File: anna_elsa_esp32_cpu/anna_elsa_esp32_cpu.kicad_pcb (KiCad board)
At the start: 4 copper layers, 170.2 x 106.7 mm, 115 parts, among them J1 REEL_RIGHT, J10 CREDIT_DISPLAY, J11 SPKR_R, J12 HEADER_6x2, J14 DOOR_SW, J2 REEL_CENTRE, J22 BTN_SWITCHES, J23 BTN_LAMPS, J3 REEL_LEFT, J4 LED / VFD, J5 LED_STRIP, J6 ATX-24, J7 HOPPER, J8 COIN_VALIDATOR, J9 SPKR_L, Q1 BC846, Q2 BC856, Q3 ULN2803ADWR, Q4 BSS138, Q7 BSS138, SW1 RESET, SW2 BOOT, U1 ESP32-WROOM-32E(16M), U10 SN74LVC1G17, U11 SN74LVC1G17, U12 Boost_Converter, U2 SN74LVC1G17, U3 TAS5825MRHB, U4 DS3231M, U5 SN74LVC1G17, U6 SN74LVC1G17, U7 SN74LVC1G17, U8 MCP23017-E_SO, U9 SN74LVC1G17

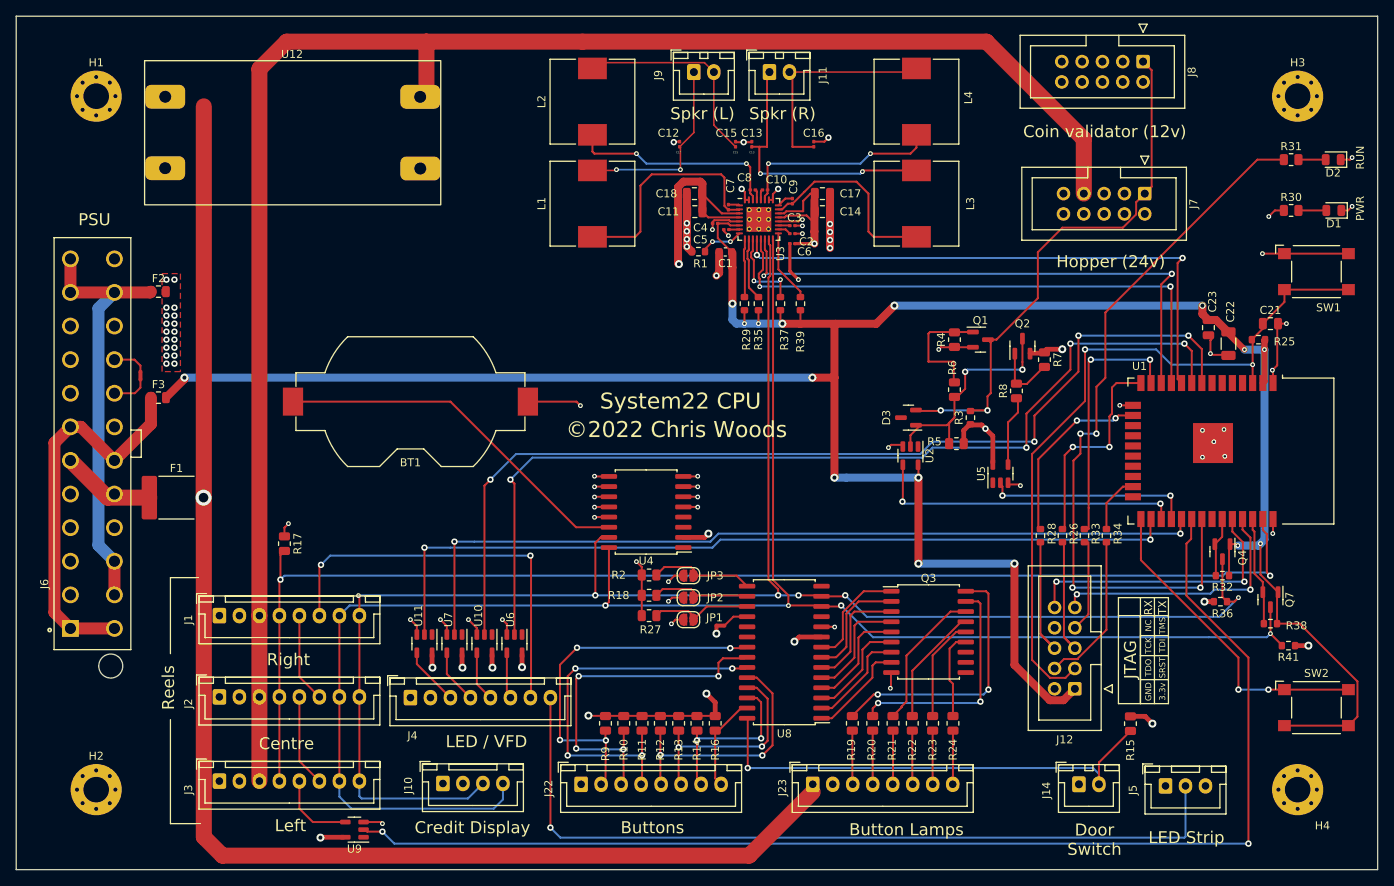
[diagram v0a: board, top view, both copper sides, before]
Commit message: Added current cpu pcb and removed old
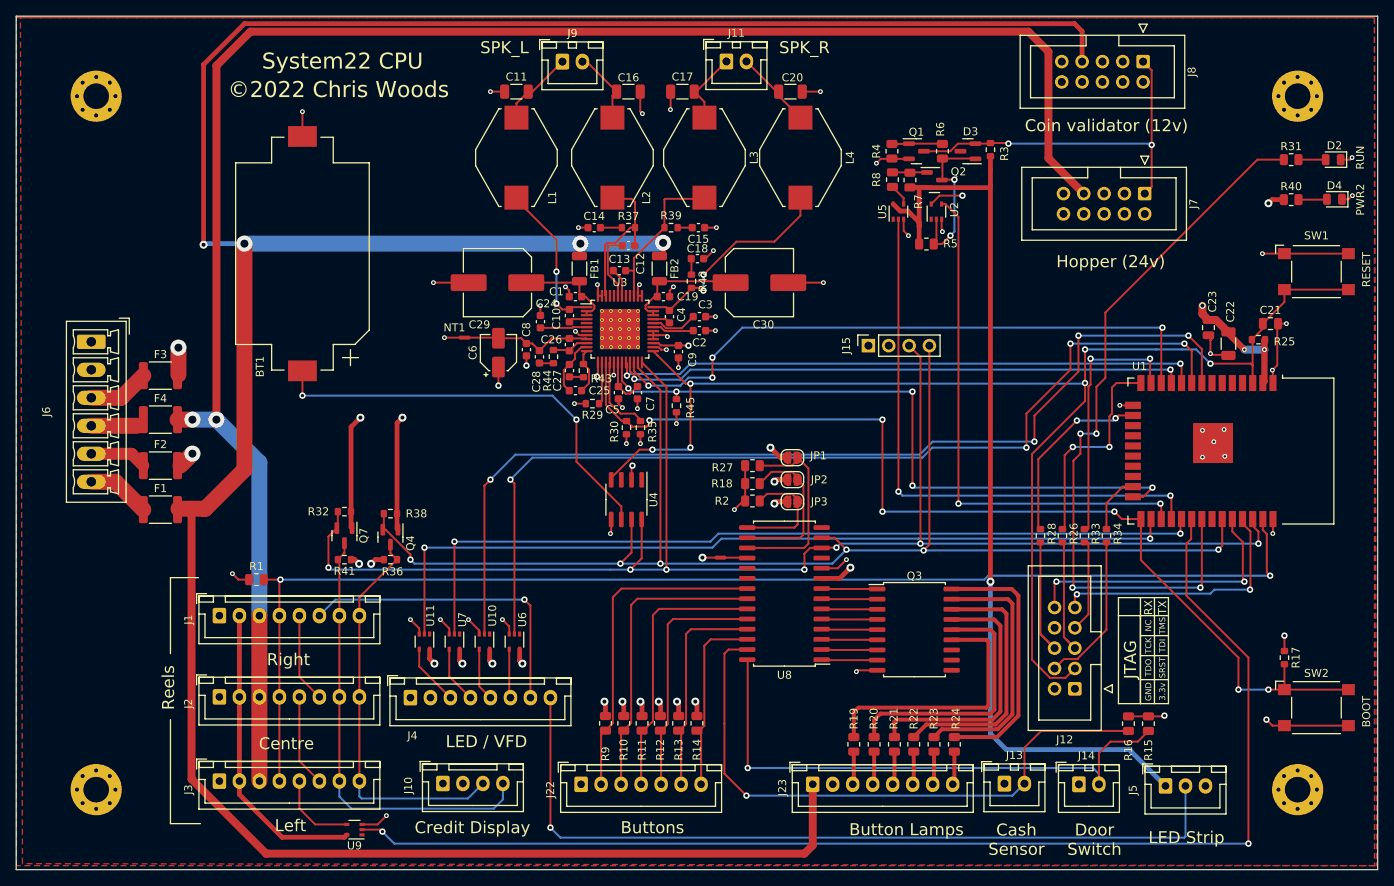
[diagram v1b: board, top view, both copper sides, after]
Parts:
- removed D1: PWR, LED_SMD:LED_0805_2012Metric
- removed U12: Boost_Converter, Converter_DCDC:Boost_Converter
- added C19: 100nF/50v, Capacitor_SMD:C_0603_1608Metric, F.Cu at (126.6, 55.4)
- added C20: 680nF/50V, Capacitor_SMD:C_1206_3216Metric, F.Cu at (142.5, 29.8)
- added C24: 220pF/50V, Capacitor_SMD:C_0603_1608Metric, F.Cu at (111.2, 58.5)
- added C25: 4.7nF/50V, Capacitor_SMD:C_0603_1608Metric, F.Cu at (115.6, 67.1)
- added C26: 4.7nF/50V, Capacitor_SMD:C_0603_1608Metric, F.Cu at (114.9, 61.4)
- added C27: 47nF/16v, Capacitor_SMD:C_0603_1608Metric, F.Cu at (114.9, 64.6)
- added C28: 47nF/16v, Capacitor_SMD:C_0603_1608Metric, F.Cu at (111.1, 62.9)
- added C29: 220µF/35v, Capacitor_SMD:C_Elec_8x10.2, F.Cu at (105.9, 53.6)
- added C30: 220µF/35v, Capacitor_SMD:C_Elec_8x10.2, F.Cu at (138.6, 53.6)
- added D4: PWR2, LED_SMD:LED_0805_2012Metric, F.Cu at (210.5, 43.2)
- added F4: 2A 30V, Fuse:Fuse_1812_4532Metric, F.Cu at (63.8, 70.8)
- added FB1: 120Ohm@100MHz 4A, Inductor_SMD:L_1206_3216Metric, F.Cu at (116.1, 51.9)
- added FB2: 120Ohm@100MHz 4A, Inductor_SMD:L_1206_3216Metric, F.Cu at (126.1, 51.9)
- added J13: CASH_LVL, Connector_JST:JST_XH_B2B-XH-A_1x02_P2.50mm_Vertical, F.Cu at (169.2, 116.2)
- added J15: Oled, Connector_PinSocket_2.54mm:PinSocket_1x04_P2.54mm_Vertical, F.Cu at (152.2, 61.5)
- added R40: 180, Resistor_SMD:R_0805_2012Metric, F.Cu at (205.1, 43.2)
- added R42: 18, Resistor_SMD:R_0603_1608Metric, F.Cu at (130.1, 53.5)
- added R43: 470, Resistor_SMD:R_0603_1608Metric, F.Cu at (116.6, 64.6)
- added R44: 470, Resistor_SMD:R_0603_1608Metric, F.Cu at (112.9, 62.9)
- added R45: 10k, Resistor_SMD:R_0603_1608Metric, F.Cu at (128.2, 69.0)
- BT1: footprint Battery:BatteryHolder_Keystone_1058_1x2032 -> Battery:BatteryHolder_Keystone_1060_1x2032
- C1: value 4.7µF/16v -> 100nF/50v
- C10: value 0.47µF -> 33nF/50V; footprint Capacitor_SMD:C_0201_0603Metric -> Capacitor_SMD:C_0603_1608Metric
- C11, C17: value 22µF/35v -> 680nF/50V; footprint Capacitor_SMD:C_0805_2012Metric -> Capacitor_SMD:C_1206_3216Metric
- C12, C13: value 0.68µF -> 33nF/50V; footprint Capacitor_SMD:C_0201_0603Metric -> Capacitor_SMD:C_0603_1608Metric
- C14, C18: value 22µF/35v -> 330pF/50V; footprint Capacitor_SMD:C_0805_2012Metric -> Capacitor_SMD:C_0603_1608Metric
- C15: value 0.68µF -> 330pF/50V; footprint Capacitor_SMD:C_0201_0603Metric -> Capacitor_SMD:C_0603_1608Metric
- C16: value 0.68µF -> 680nF/50V; footprint Capacitor_SMD:C_0201_0603Metric -> Capacitor_SMD:C_1206_3216Metric
- C2, C3: value 1µF -> 100nF/50v; footprint Capacitor_SMD:C_0201_0603Metric -> Capacitor_SMD:C_0603_1608Metric
- C23: value 1µF/50V -> 1µF/50v
- C4: value 0.1µF/16v -> 33nF/50V; footprint Capacitor_SMD:C_0201_0603Metric -> Capacitor_SMD:C_0603_1608Metric
- C5: value 1µF -> 4.7µF/16v; footprint Capacitor_SMD:C_0201_0603Metric -> Capacitor_SMD:C_0603_1608Metric
- C6: value 0.1µF/16v -> 10µF/6.3v; footprint Capacitor_SMD:C_0201_0603Metric -> Capacitor_SMD:CP_Elec_4x5.4
- C7, C8, C9: value 0.47µF -> 100nF/50v; footprint Capacitor_SMD:C_0201_0603Metric -> Capacitor_SMD:C_0603_1608Metric
- F1: value 2A 15V -> 2A 30V; footprint Fuse:Fuse_2920_7451Metric -> Fuse:Fuse_1812_4532Metric
- F2: value 2.6A 6V -> 2A 30V; footprint Fuse:Fuse_0805_2012Metric -> Fuse:Fuse_1812_4532Metric
- F3: value Polyfuse -> 2A 30V; footprint Fuse:Fuse_0805_2012Metric -> Fuse:Fuse_1812_4532Metric
- J11: value SPKR_R -> SPK_R
- J12: value HEADER_6x2 -> JTAG
- J22: footprint Connector_JST:JST_XH_B8B-XH-A_1x08_P2.50mm_Vertical -> Connector_JST:JST_XH_B7B-XH-A_1x07_P2.50mm_Vertical
- J6: value ATX-24 -> PSU; footprint Connector_TE-Connectivity:TE_1-1775099-3 -> Connector_Phoenix_MC:PhoenixContact_MCV_1,5_6-G-3.5_1x06_P3.50mm_Vertical
- J9: value SPKR_L -> SPK_L
- L1, L2, L3, L4: value 10µH / 4.4A / 0.03Ohm -> 15µH; footprint Inductor_SMD:L_10.4x10.4_H4.8 -> Inductor_SMD:L_SigTra_SC3316F
- Q1: value BC846 -> SS8050
- Q2: value BC856 -> SS8850
- R1: value 0 -> 4k7; footprint Resistor_SMD:R_0603_1608Metric -> Resistor_SMD:R_0805_2012Metric
- R17: value 4k7 -> 10k; footprint Resistor_SMD:R_0805_2012Metric -> Resistor_SMD:R_0603_1608Metric
- R29: value 10k -> 15.0k
- R30: value 220 -> 10k; footprint Resistor_SMD:R_0805_2012Metric -> Resistor_SMD:R_0603_1608Metric
- R35: value 10k -> 18.2k
- R37, R39: value 10k -> 18
- U1: value ESP32-WROOM-32E(16M) -> ESP32-WROOM-32D(16M)
- U10, U11, U2, U5, U6, U7, U9: footprint Package_TO_SOT_SMD:SOT-23-5 -> Package_TO_SOT_SMD:SOT-353_SC-70-5
- U3: value TAS5825MRHB -> TAS5731PHP; footprint Package_DFN_QFN:VQFN-32-1EP_5x5mm_P0.5mm_EP3.1x3.1mm_ThermalVias -> Package_QFP:TQFP-48-1EP_7x7mm_P0.5mm_EP5x5mm_ThermalVias
- U4: footprint Package_SO:SOIC-16W_7.5x10.3mm_P1.27mm -> Package_SO:SOIC-8_3.9x4.9mm_P1.27mm
- U8: value MCP23017-E_SO -> MCP23017T-E/SO
- moved R17 125.8 mm to (204.2, 100.5)
- moved R41 118.5 mm to (86.8, 88.2)
- moved R38 116.6 mm to (86.8, 82.2)
- moved Q7 116.0 mm to (86.8, 85.2)
- moved R32 104.3 mm to (92.5, 82.5)
- moved Q4 104.0 mm to (92.5, 85.4)
- moved R36 103.9 mm to (92.5, 88.2)
- moved R30 87.4 mm to (122.0, 71.8), turned to 90 degrees
- moved R1 68.8 mm to (75.8, 90.8), turned to 0 degrees
- moved R16 51.7 mm to (184.8, 108.8)
- moved NT1 40.8 mm to (101.8, 60.5), turned to 0 degrees
- moved C6 39.2 mm to (106.0, 62.4), turned to 90 degrees
- moved U5 35.1 mm to (156.0, 44.8)
- moved C8 34.6 mm to (109.5, 62.0), turned to 90 degrees
- moved D3 34.1 mm to (164.7, 37.2)
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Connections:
- BT1 pad 1: /VBAT -> /ESP32-Wroom/VBAT
- C1 pad 1: +3V3 -> PVDD1
- C10 pad 1: /Audio/BST_B- -> Net-(C10-Pad1)
- C10 pad 2: /Audio/OUT_B- -> Net-(C10-Pad2)
- C11 pad 1: +12V -> GND
- C11 pad 2: GND -> Net-(C11-Pad2)
- C12 pad 1: /Audio/OUTL+ -> Net-(C12-Pad1)
- C12 pad 2: GND -> Net-(C12-Pad2)
- C13 pad 1: /Audio/OUTR+ -> Net-(C13-Pad1)
- C13 pad 2: GND -> Net-(C13-Pad2)
- C14 pad 1: +12V -> GND
- C14 pad 2: GND -> Net-(C14-Pad2)
- C15 pad 1: /Audio/OUTL- -> GND
- C15 pad 2: GND -> Net-(C15-Pad2)
- C16 pad 1: /Audio/OUTR- -> GND
- C16 pad 2: GND -> Net-(C16-Pad2)
- C17 pad 1: +12V -> GND
- C17 pad 2: GND -> Net-(C17-Pad2)
- C18 pad 1: +12V -> GND
- C18 pad 2: GND -> Net-(C18-Pad2)
- C2 pad 1: GND -> Net-(C2-Pad1)
- C2 pad 2: Net-(C2-Pad2) -> GND
- C21 pad 1: JTAG_SRST -> ~{RST}
- C22 pad 1: +3V3 -> +3.3V
- C23 pad 1: +3V3 -> +3.3V
- C3 pad 1: GND -> Net-(C3-Pad1)
- C3 pad 2: Net-(C3-Pad2) -> GND
- C4 pad 1: +3V3 -> Net-(C4-Pad1)
- C4 pad 2: GND -> Net-(C4-Pad2)
- C5 pad 1: GND -> Net-(C5-Pad1)
- C5 pad 2: Net-(C5-Pad2) -> GND
- C6 pad 1: +12V -> +3.3V
- C6 pad 2: GND -> VSSA
- C7 pad 1: /Audio/OUT_A+ -> Net-(C5-Pad1)
- C7 pad 2: /Audio/BST_A+ -> GND
- C8 pad 1: /Audio/BST_A- -> +3.3V
- C8 pad 2: /Audio/OUT_A- -> VSSA
- C9 pad 1: /Audio/OUT_B+ -> +3.3V
- C9 pad 2: /Audio/BST_B+ -> GND
- F3 pad 2: +3V3 -> +3.3V
- J11 pad 1: /Audio/OUTR+ -> Net-(C17-Pad2)
- J11 pad 2: /Audio/OUTR- -> Net-(C20-Pad2)
- J12 pad 1: +3V3 -> +3.3V
- J12 pad 3: JTAG_SRST -> ~{RST}
- J6 pad 1: Net-(F3-Pad1) -> GND
- J6 pad 2: Net-(F3-Pad1) -> unconnected-(J6-Pad2)
- J6 pad 3: GND -> Net-(F3-Pad1)
- J6 pad 4: Net-(F2-Pad1) -> Net-(F4-Pad1)
- J6 pad 5: GND -> Net-(F2-Pad1)
- J6 pad 6: Net-(F2-Pad1) -> Net-(F1-Pad1)
- J7 pad 10: +24V -> unconnected-(J7-Pad10)
- J7 pad 2: unconnected-(J7-Pad2) -> GND
- J8 pad 10: +12V -> unconnected-(J8-Pad10)
- J8 pad 2: unconnected-(J8-Pad2) -> GND
- J9 pad 1: /Audio/OUTL+ -> Net-(C11-Pad2)
- J9 pad 2: /Audio/OUTL- -> Net-(C16-Pad2)
- JP1 pad 2: +5V -> +3.3V
- JP2 pad 2: +5V -> +3.3V
- JP3 pad 2: +5V -> +3.3V
- L1 pad 1: /Audio/OUT_A+ -> Net-(C10-Pad1)
- L1 pad 2: /Audio/OUTL+ -> Net-(C11-Pad2)
- L2 pad 1: /Audio/OUT_A- -> Net-(C12-Pad2)
- L2 pad 2: /Audio/OUTL- -> Net-(C16-Pad2)
- L3 pad 1: /Audio/OUT_B+ -> Net-(C13-Pad2)
- L3 pad 2: /Audio/OUTR+ -> Net-(C17-Pad2)
- L4 pad 1: /Audio/OUT_B- -> Net-(C4-Pad2)
- L4 pad 2: /Audio/OUTR- -> Net-(C20-Pad2)
- NT1 pad 1: Net-(J6-Pad16) -> GND
- NT1 pad 2: GND -> VSSA
- NT2 pad 1: +5V -> +3.3V
- Q4 pad 1: +3V3 -> +3.3V
- Q7 pad 1: +3V3 -> +3.3V
- R1 pad 1: /Audio/ADR -> GND
- R1 pad 2: GND -> EN_PWM
- R10 pad 2: +5V -> +3.3V
- R11 pad 2: +5V -> +3.3V
- R12 pad 2: +5V -> +3.3V
- R13 pad 2: +5V -> +3.3V
- R14 pad 2: +5V -> +3.3V
- R15 pad 2: +5V -> +3.3V
- R16 pad 1: Net-(J22-Pad8) -> Net-(J13-Pad2)
- R16 pad 2: +5V -> +3.3V
- R17 pad 1: GND -> +3.3V
- R17 pad 2: EN_PWM -> MCLK
- R19 pad 2: Net-(Q3-Pad18) -> Net-(Q3-Pad13)
- R20 pad 2: Net-(Q3-Pad17) -> Net-(Q3-Pad14)
- R21 pad 2: Net-(Q3-Pad16) -> Net-(Q3-Pad15)
- R22 pad 2: Net-(Q3-Pad15) -> Net-(Q3-Pad16)
- R23 pad 2: Net-(Q3-Pad14) -> Net-(Q3-Pad17)
- R24 pad 2: Net-(Q3-Pad13) -> Net-(Q3-Pad18)
- R25 pad 1: +3V3 -> +3.3V
- R25 pad 2: JTAG_SRST -> ~{RST}
- R29 pad 1: +3V3 -> /Audio/A_SEL
- R29 pad 2: Net-(U3-Pad9) -> GND
- R30 pad 1: +5V -> GND
- R30 pad 2: Net-(D1-Pad2) -> MCLK
- R32 pad 1: +3V3 -> +3.3V
- R35 pad 1: +3V3 -> Net-(R35-Pad1)
- R35 pad 2: Net-(U3-Pad10) -> GND
- R37 pad 1: +3V3 -> Net-(C14-Pad2)
- R37 pad 2: Net-(U3-Pad11) -> Net-(C12-Pad2)
- R38 pad 1: +3V3 -> +3.3V
- R39 pad 1: +3V3 -> Net-(C15-Pad2)
- R39 pad 2: Net-(U3-Pad17) -> Net-(C13-Pad2)
- R9 pad 2: +5V -> +3.3V
- SW1 pad 2: JTAG_SRST -> ~{RST}
- SW2 pad 1: Net-(SW2-Pad1) -> MCLK
- SW2 pad 2: +3V3 -> GND
- U1 pad 2: +3V3 -> +3.3V
- U1 pad 24: unconnected-(U1-Pad24) -> ~{AUDIO_PDN}
- U1 pad 25: Net-(SW2-Pad1) -> MCLK
- U1 pad 3: JTAG_SRST -> ~{RST}
- U2 pad 5: +3V3 -> +3.3V
- U3 pad 1: /Audio/BST_A+ -> Net-(C10-Pad1)
- U3 pad 10: Net-(U3-Pad10) -> /Audio/PLL_FLTM
- U3 pad 11: Net-(U3-Pad11) -> /Audio/PLL_FLTP
- U3 pad 12: AUDIO_LRCLK -> /Audio/VR_ANA
- U3 pad 13: AUDIO_SCLK -> +3.3V
- U3 pad 14: AUDIO_SDIN -> /Audio/A_SEL
- U3 pad 15: SDA -> MCLK
- U3 pad 16: SCL -> Net-(R35-Pad1)
- U3 pad 17: Net-(U3-Pad17) -> GND
- U3 pad 18: Net-(C2-Pad2) -> Net-(C5-Pad1)
- U3 pad 19: Net-(C3-Pad2) -> ~{AUDIO_PDN}
- U3 pad 2: /Audio/OUT_A+ -> PVDD1
- U3 pad 20: GND -> AUDIO_LRCLK
- U3 pad 21: +12V -> AUDIO_SCLK
- U3 pad 22: +12V -> AUDIO_SDIN
- U3 pad 23: /Audio/OUT_B+ -> SDA33
- U3 pad 24: /Audio/BST_B+ -> SCL33
- U3 pad 25: GND -> ~{RST}
- U3 pad 27: /Audio/OUT_B- -> +3.3V
- U3 pad 28: /Audio/BST_B- -> GND
- U3 pad 29: /Audio/BST_A- -> GND
- U3 pad 3: +12V -> PVDD1
- U3 pad 30: /Audio/OUT_A- -> GND
- U3 pad 31: GND -> Net-(C2-Pad1)
- U3 pad 32: GND -> Net-(C3-Pad1)
- U3 pad 33: GND -> Net-(C4-Pad1)
- U3 pad 4: +12V -> Net-(C10-Pad2)
- U3 pad 5: GND -> unconnected-(U3-Pad5)
- U3 pad 6: +3V3 -> Net-(C24-Pad2)
- U3 pad 7: Net-(C5-Pad2) -> unconnected-(U3-Pad7)
- U3 pad 8: /Audio/ADR -> GND
- U3 pad 9: Net-(U3-Pad9) -> VSSA
- U4 pad 2: +5V -> +3.3V
- U4 pad 4: unconnected-(U4-Pad4) -> ~{RST}
- U4 pad 6: GND -> /ESP32-Wroom/VBAT
- U4 pad 7: GND -> SDA33
- U4 pad 8: GND -> SCL33
- U8 pad 12: SCL -> SCL33
- U8 pad 13: SDA -> SDA33
- U8 pad 27: Net-(J22-Pad8) -> Net-(J13-Pad2)
- U8 pad 9: +5V -> +3.3V
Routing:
- net +3V3: track 331.0 -> 0.00 mm, vias 16 -> 0
- net SCL33: track 13.7 -> 189.1 mm, vias 0 -> 7
- net SCL: track 224.3 -> 55.6 mm, vias 4 -> 0
- net SDA33: track 7.51 -> 175.5 mm, vias 0 -> 6
- net ~{RST}: track 0.00 -> 166.9 mm, vias 0 -> 6
- net SDA: track 214.5 -> 50.1 mm, vias 6 -> 0
- net MCLK: track 0.00 -> 129.1 mm, vias 0 -> 6
- net +5V: track 64.4 -> 170.0 mm, vias 37 -> 8
- net +3.3V: track 0.00 -> 96.1 mm, vias 0 -> 26
- net JTAG_SRST: track 91.4 -> 0.00 mm, vias 2 -> 0
- net +12V: track 448.9 -> 361.7 mm, vias 3 -> 4
- net ~{AUDIO_PDN}: track 0.00 -> 84.9 mm, vias 0 -> 5
- net Net-(J13-Pad2): track 0.00 -> 75.7 mm, vias 0 -> 1
- net /ESP32-Wroom/VBAT: track 0.00 -> 53.4 mm, vias 0 -> 2
- net Net-(F2-Pad1): track 53.8 -> 7.12 mm
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- added copper zone on In2.Cu, net +3.3V
- added copper zone on F.Cu, net GND
- removed copper zone on F.Cu, net +5V
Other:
- board text added: "Cash Sensor"
- board text removed: "PSU"
- board text removed: "Spkr (L)"
- board text removed: "Spkr (R)"

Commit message: Latest schematics
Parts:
- removed D3: BAT54, Package_TO_SOT_SMD:SOT-23
- added D1: BAT54W, Package_TO_SOT_SMD:SOT-323_SC-70, F.Cu at (165.0, 37.2)
- C24: value 220pF/50V -> 2.2nF/50V
- R32, R36, R38, R41: value 10k -> 4k7
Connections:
- J7 pad 2: GND -> unconnected-(J7-Pad2)
- J8 pad 2: GND -> unconnected-(J8-Pad2)
- Q2 pad 3: HOST_RX -> Net-(Q2-Pad3)
- R6 pad 1: HOST_RX -> Net-(Q2-Pad3)
- U3 pad 25: ~{RST} -> JTAG_TMS
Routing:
- net JTAG_TMS: track 11.4 -> 87.3 mm, vias 0 -> 2
- net ~{RST}: track 166.9 -> 160.6 mm
- net HOST_RX: track 21.4 -> 16.0 mm
- net Net-(Q2-Pad3): track 0.00 -> 2.71 mm
